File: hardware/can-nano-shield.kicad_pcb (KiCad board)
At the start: 2 copper layers, 18.1 x 43.6 mm, 20 parts, among them J1 Conn_01x15_Socket, J2 Conn_01x15_Socket, J3 Conn_01x04_Pin, J4 Screw_Terminal_01x03, U1 MCP2515-xSO, U2 TJA1051T-3, Y2 16MHz 9pF

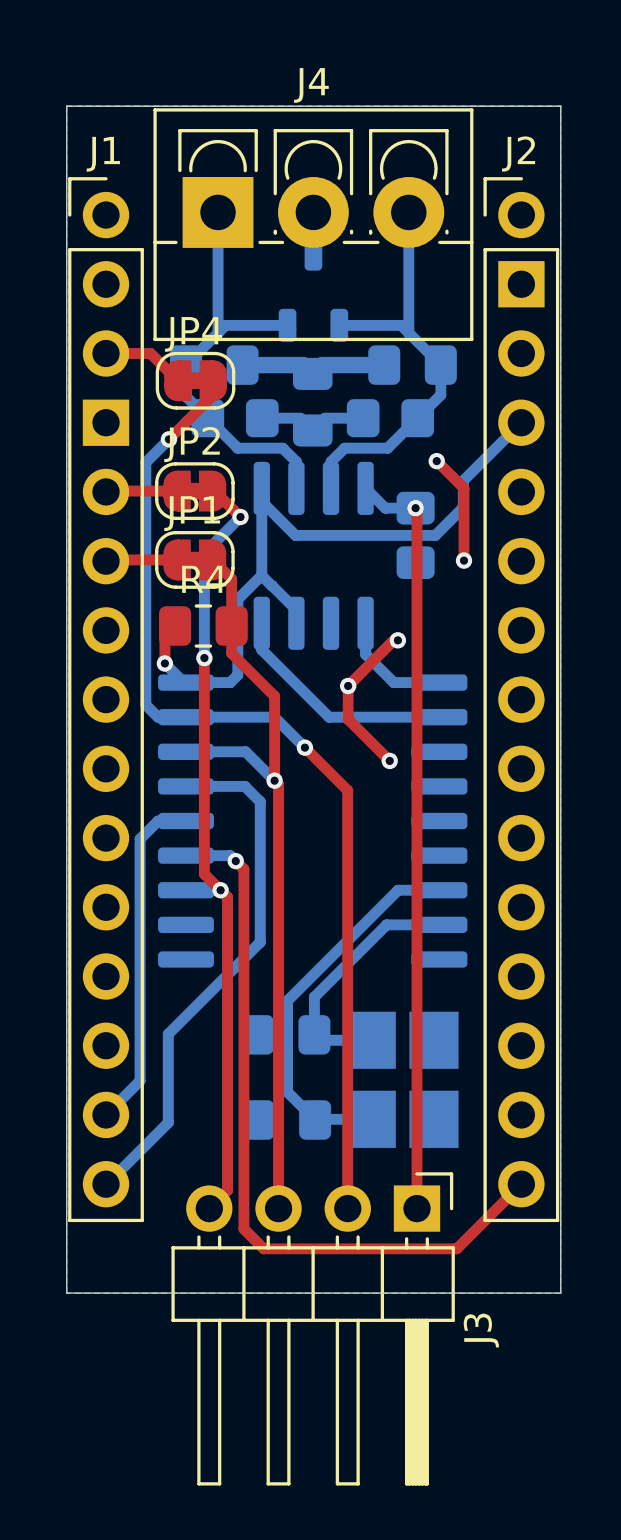
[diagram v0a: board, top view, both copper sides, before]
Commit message: updated with cmc inductor + esd diode + emc caps on H L inputs
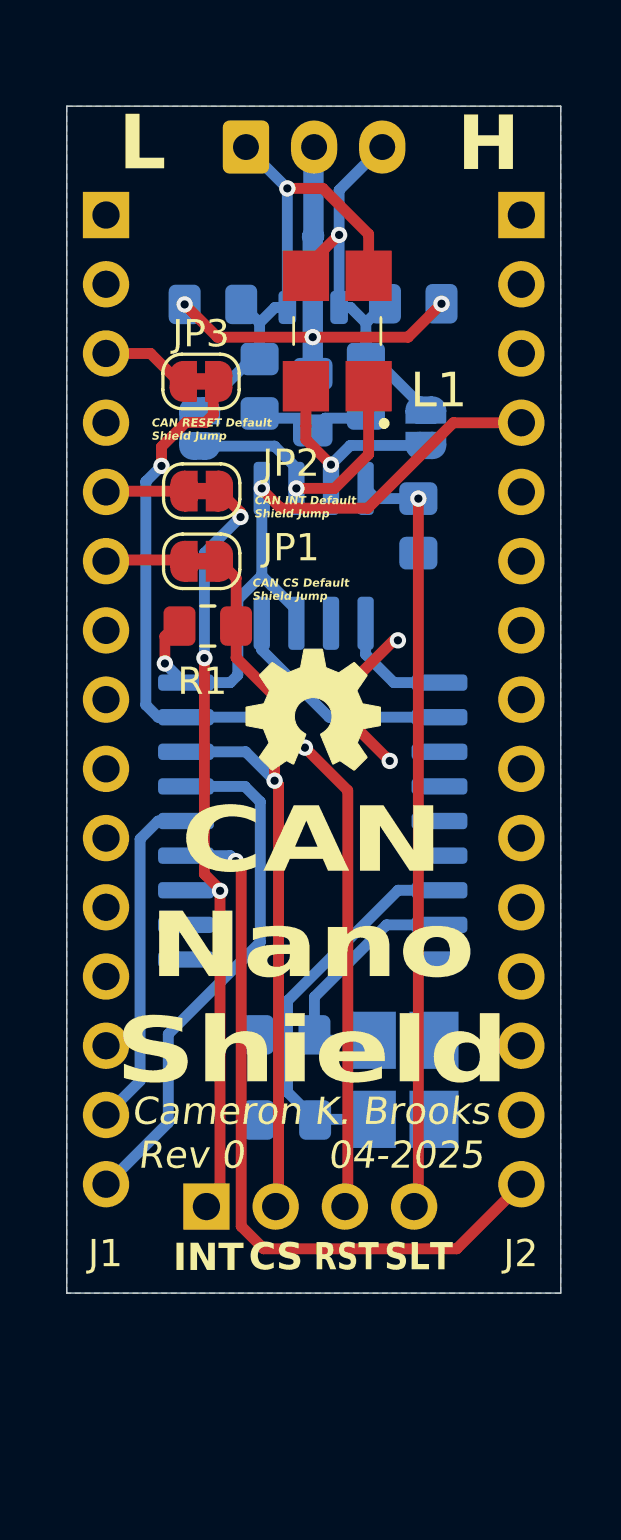
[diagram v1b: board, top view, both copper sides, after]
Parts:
- removed D2: PESD2CANFD24LT-Q, Package_TO_SOT_SMD:TSOT-23
- removed R7: 60, Resistor_SMD:R_0805_2012Metric_Pad1.20x1.40mm_HandSolder
- added D1: PESD2CANFD24LT-Q, Package_TO_SOT_SMD:TSOT-23, B.Cu at (145.9, 79.7)
- added JP4: SolderJumper_2_Open, Jumper:SolderJumper-2_P1.3mm_Open_RoundedPad1.0x1.5mm, B.Cu at (150.1, 85.4)
- added JP5: SolderJumper_2_Open, Jumper:SolderJumper-2_P1.3mm_Open_RoundedPad1.0x1.5mm, B.Cu at (141.8, 85.4)
- added L1: B82789C0104N002, kml-custom:B82789C0113N002, F.Cu at (147.1, 81.8)
- added Ref**: Val**, SparkFun-Aesthetic:OSHW_Logo_5mm, F.Cu at (145.9, 96.0)
- added Rt2: 60, Resistor_SMD:R_0805_2012Metric_Pad1.20x1.40mm_HandSolder, B.Cu at (143.9, 83.9)
- J1, J2, J3: moved to B.Cu
- J4: value Screw_Terminal_01x03 -> Conn_01x03_Socket; footprint TerminalBlock_4Ucon:TerminalBlock_4Ucon_1x03_P3.50mm_Vertical -> Connector_JST:JST_XH_S3B-XH-A-1_1x03_P2.50mm_Horizontal; moved to B.Cu
- moved J3 7.73 mm to (142.0, 114.0)
- moved J4 2.61 mm to (143.4, 75.1)
- moved C4 2.25 mm to (149.6, 80.8)
- moved C5 2.23 mm to (142.2, 80.9), turned to 180 degrees
- moved Rt1 1.48 mm to (147.8, 83.9), turned to -90 degrees
- moved R2 0.36 mm to (149.8, 89.0)
- moved JP1 0.25 mm to (141.8, 90.3)
- moved JP2 0.25 mm to (141.8, 87.7)
- moved JP3 0.20 mm to (141.8, 83.7)
- moved R1 0.16 mm to (142.1, 92.7)
- turned J1 to 180 degrees
- turned J2 to 180 degrees
- renumbered C6 to C1, C7 to C2, C4 to C3, C2 to C4, C3 to C5, JP4 to JP3, R4 to R1, R5 to R2, R2 to Rt1, Y2 to Y1
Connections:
- C4 pad 1: /CAN_H -> GND
- C4 pad 2: GND -> /CAN_H
- J2 pad 1: /VIN -> unconnected-(J2-Pin_1-Pad1)
- J3 pad 1: /SILENT -> /~{CAN_INT}
- J3 pad 2: /CAN_RESET -> /CAN_CS
- J3 pad 3: /CAN_CS -> /CAN_RESET
- J3 pad 4: /~{CAN_INT} -> /SILENT
- U2 pad 6: /CAN_L -> /CAN_L_IN
- U2 pad 7: /CAN_H -> /CAN_H_IN
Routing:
- net /CAN_L_IN: track 0.00 -> 10.3 mm, vias 0 -> 1
- net GND: track 15.4 -> 24.7 mm, vias 5 -> 6
- net /CAN_H_IN: track 0.00 -> 7.90 mm, vias 0 -> 1
- net /CAN_L: track 16.1 -> 18.2 mm, vias 0 -> 1
- net +5V: track 27.6 -> 26.0 mm, vias 1 -> 2
- net /CAN_H: track 16.0 -> 15.1 mm, vias 0 -> 1
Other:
- board text added: "CAN CS Default Shield Jump"
- board text added: "CAN INT Default Shield Jump"
- board text added: "CAN Nano Shield"
- board text added: "CAN RESET Default Shield Jump"
- board text added: "CAN_H CMC Bypass Jump"
- board text added: "CS"
- board text added: "Cameron K. Brooks Rev 0 04-2025"
- board text added: "H"
- board text added: "INT"
- board text added: "L"
- board text added: "RST"
- board text added: "SLT"

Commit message: added outputs
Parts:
- removed L1: B82789C0104N002, kml-custom:B82789C0113N002
- added T1: B82789C0113N002, kml-custom:SMT_13N002_TDK, F.Cu at (147.1, 93.2)
- J1, J2: value Conn_01x15_Socket -> SSQ-115-03-T-S; footprint Connector_PinHeader_2.54mm:PinHeader_1x15_P2.54mm_Vertical -> kml-custom:SAMTEC_SSQ-115-03-T-S; moved to F.Cu
- J4: moved to F.Cu
- R1: footprint Capacitor_SMD:C_0805_2012Metric_Pad1.18x1.45mm_HandSolder -> Resistor_SMD:R_0805_2012Metric_Pad1.20x1.40mm_HandSolder
- moved J3 37.2 mm to (115.0, 88.4), turned to 180 degrees
- moved C1 33.1 mm to (118.2, 91.3), turned to 90 degrees
- moved Y1 32.6 mm to (119.7, 95.6), turned to 0 degrees
- moved J2 29.9 mm to (133.6, 99.9)
- moved C2 28.7 mm to (121.3, 91.3), turned to 90 degrees
- moved J4 22.2 mm to (153.8, 94.8), turned to 90 degrees
- moved U1 18.4 mm to (129.2, 92.3), turned to 90 degrees
- moved C4 15.2 mm to (148.2, 96.0), turned to 90 degrees
- moved Ref** 13.4 mm to (133.0, 92.3), turned to -90 degrees
- moved D1 13.1 mm to (149.3, 92.3), turned to 0 degrees
- moved JP1 12.8 mm to (143.6, 96.4), turned to 0 degrees
- moved R2 12.1 mm to (140.0, 96.2), turned to 180 degrees
- moved Rt1 10.7 mm to (145.1, 94.2), turned to 180 degrees
- moved C5 9.72 mm to (148.1, 88.6), turned to 90 degrees
- moved J1 8.51 mm to (133.6, 84.7)
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- renumbered JP4 to JP1, JP5 to JP2, JP1 to JP3, JP2 to JP4, JP3 to JP5
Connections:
- J4 pad 1: /CAN_L -> /CAN_H
- J4 pad 3: /CAN_H -> /CAN_L
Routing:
- net GND: track 24.7 -> 14.1 mm, vias 6 -> 3
- net /CAN_L_IN: track 10.3 -> 7.32 mm
- net /CAN_L: track 18.2 -> 16.5 mm
- net /CAN_H: track 15.1 -> 16.4 mm
- net /CAN_H_IN: track 7.90 -> 7.09 mm
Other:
- board size 18.1 x 43.6 mm -> 50 x 18 mm
- board text added: "CAN CS Closed Jump"
- board text added: "CAN INT Closed Jump"
- board text added: "CAN RESET Closed Jump"
- board text removed: "CAN CS Default Shield Jump"
- board text removed: "CAN INT Default Shield Jump"
- board text removed: "CAN RESET Default Shield Jump"
